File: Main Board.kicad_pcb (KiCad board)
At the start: 4 copper layers, 161 x 92 mm, 369 parts, among them J1 Motor Y, J10 CA58SUB-B, J11 PC6 EPSON MAINBOARD, J12 Y AXIS, J13 Z AXIS, J14 LED 1, J15 LED 2, J16 Power Input, J17 VS, J18 12V, J19 5V, J2 Motor Z, J20 3.3V, J21 TABLE SENSOR, J22 INPUT1, J23 INPUT2, J24 PHOTO SENSOR EMITER, J25 PHOTO SENSOR RECEIVER, J26 ANALOG, J27 INPUT3, J28 OUT1, J29 OUT2, J3 USB_B, J30 RELAY, J31 EMERGENCY, J32 EPSON POWER IN, J33 EPSON BOARD POWER, J34 Display, J35 SPI Interface, J36 I2C Interface, J37 LED4, J38 LED3, J39 Key 3, J4 SWD, J40 Key 4, J41 Key 1, J42 Key 2, J5 DEBUG, J6 LIMIT Y BACK, J7 LIMIT Y FRONT, J8 LIMIT Z UP, J9 LIMIT Z DOWN, K1 S13-24V-2C, Q1 2N7002K, Q10 2N7002K, Q11 BC817, Q12 BC817, Q13 BC817, Q14 2N7002K, Q15 2N7002K, Q16 2N7002K, Q17 BC817, Q18 2N7002K, Q19 2N7002K, Q2 2N7002K, Q20 2N7002K, Q21 2N7002K, Q3 2N7002K, Q4 2N7002K, Q5 2N7002K, Q6 2N7002K, Q7 2N7002K, Q8 YJS9435A, Q9 2N7002K, U1 TMC2209-LA, U10 74HC2G32, U11 74HC245, U12 SHTC3, U2 TMC2209-LA, U3 STM32F401VETx, U4 USBUF02W6, U5 74HC245, U6 MCP16301, U7 A4403, U8 MCP16301, U9 MCP6002-xSN, Y1 8MHz

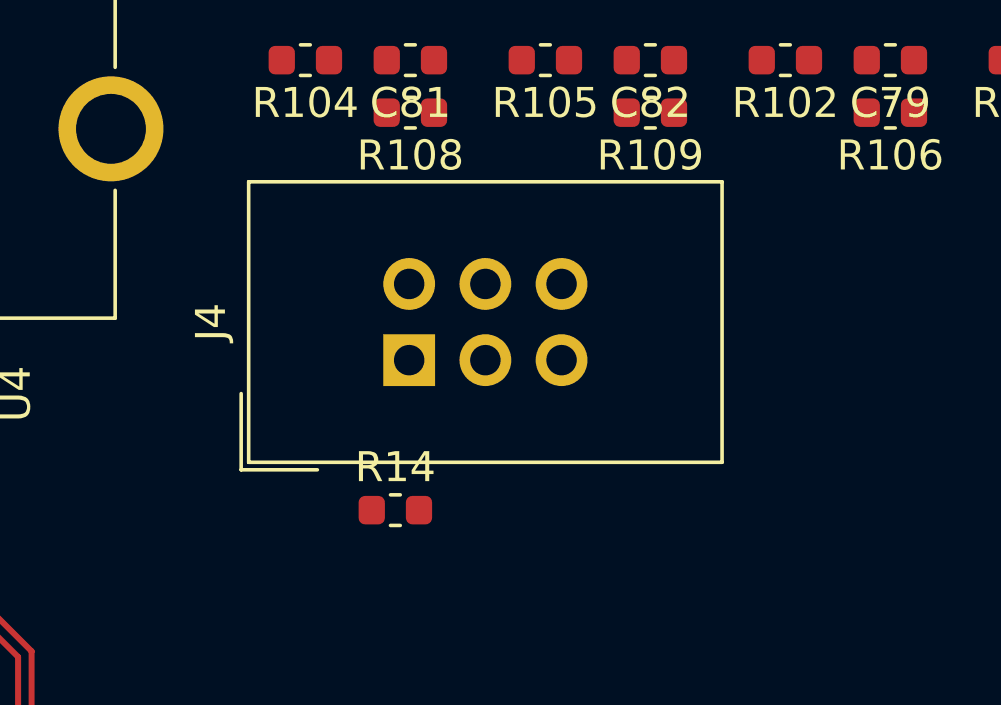
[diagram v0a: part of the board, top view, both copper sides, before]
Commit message: Change SWD IDC connector to TC2030
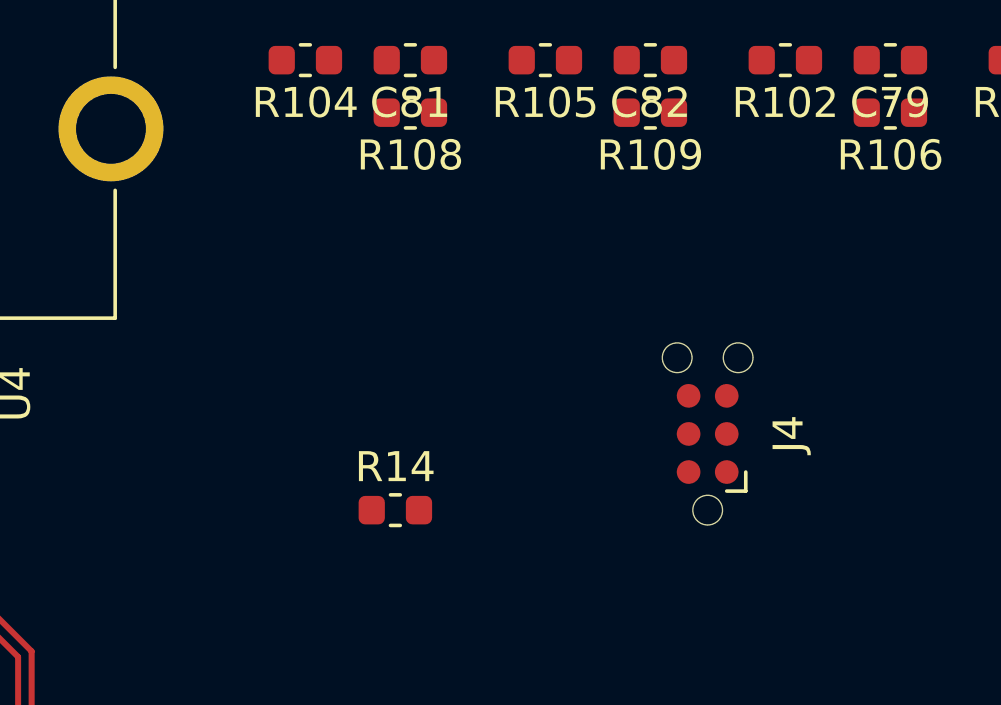
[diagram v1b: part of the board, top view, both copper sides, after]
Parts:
- J4: footprint Connector_IDC:IDC-Header_2x03_P2.54mm_Vertical -> Connector:Tag-Connect_TC2030-IDC-NL_2x03_P1.27mm_Vertical
- moved J4 10.2 mm to (156.2, 45.5)
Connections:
- J4 pad 2: NRST -> SWDIO
- J4 pad 3: SWO -> NRST
- J4 pad 4: SWDIO -> SWCLK
- J4 pad 6: SWCLK -> SWO
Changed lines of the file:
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@@
     )
   )
-  (module Connector_IDC:IDC-Header_2x03_P2.54mm_Vertical (layer F.Cu)
-    (at 146.21 43 90)
-    (descr "Through hole straight IDC box header, 2x03, 2.54mm pitch, double rows")
-    (tags "Through hole IDC box header THT 2x03 2.54mm double row")
-    (fp_text reference J4 (at 1.27 -6.604 90) (layer F.SilkS)
-      (effects (font (size 1 1) (thickness 0.15)))
-    )
-    (fp_text value SWD (at 1.27 11.684 90) (layer F.Fab)
-      (effects (font (size 1 1) (thickness 0.15)))
-    )
-    (fp_text user %R (at 1.27 2.54 90) (layer F.Fab)
-      (effects (font (size 1 1) (thickness 0.15)))
-    )
-    (fp_line (start 5.695 -5.1) (end 5.695 10.18) (layer F.Fab) (width 0.1))
-    (fp_line (start 5.145 -4.56) (end 5.145 9.62) (layer F.Fab) (width 0.1))
-    (fp_line (start -3.155 -5.1) (end -3.155 10.18) (layer F.Fab) (width 0.1))
-    (fp_line (start -2.605 -4.56) (end -2.605 0.29) (layer F.Fab) (width 0.1))
-    (fp_line (start -2.605 4.79) (end -2.605 9.62) (layer F.Fab) (width 0.1))
-    (fp_line (start -2.605 0.29) (end -3.155 0.29) (layer F.Fab) (width 0.1))
-    (fp_line (start -2.605 4.79) (end -3.155 4.79) (layer F.Fab) (width 0.1))
-    (fp_line (start 5.695 -5.1) (end -3.155 -5.1) (layer F.Fab) (width 0.1))
-    (fp_line (start 5.145 -4.56) (end -2.605 -4.56) (layer F.Fab) (width 0.1))
-    (fp_line (start 5.695 10.18) (end -3.155 10.18) (layer F.Fab) (width 0.1))
-    (fp_line (start 5.145 9.62) (end -2.605 9.62) (layer F.Fab) (width 0.1))
-    (fp_line (start 5.695 -5.1) (end 5.145 -4.56) (layer F.Fab) (width 0.1))
-    (fp_line (start 5.695 10.18) (end 5.145 9.62) (layer F.Fab) (width 0.1))
-    (fp_line (start -3.155 -5.1) (end -2.605 -4.56) (layer F.Fab) (width 0.1))
-    (fp_line (start -3.155 10.18) (end -2.605 9.62) (layer F.Fab) (width 0.1))
-    (fp_line (start 5.95 -5.35) (end 5.95 10.43) (layer F.CrtYd) (width 0.05))
-    (fp_line (start 5.95 10.43) (end -3.41 10.43) (layer F.CrtYd) (width 0.05))
-    (fp_line (start -3.41 10.43) (end -3.41 -5.35) (layer F.CrtYd) (width 0.05))
-    (fp_line (start -3.41 -5.35) (end 5.95 -5.35) (layer F.CrtYd) (width 0.05))
-    (fp_line (start 5.945 -5.35) (end 5.945 10.43) (layer F.SilkS) (width 0.12))
-    (fp_line (start 5.945 10.43) (end -3.405 10.43) (layer F.SilkS) (width 0.12))
-    (fp_line (start -3.405 10.43) (end -3.405 -5.35) (layer F.SilkS) (width 0.12))
-    (fp_line (start -3.405 -5.35) (end 5.945 -5.35) (layer F.SilkS) (width 0.12))
-    (fp_line (start -3.655 -5.6) (end -3.655 -3.06) (layer F.SilkS) (width 0.12))
-    (fp_line (start -3.655 -5.6) (end -1.115 -5.6) (layer F.SilkS) (width 0.12))
-    (pad 1 thru_hole rect (at 0 0 90) (size 1.7272 1.7272) (drill 1.016) (layers *.Cu *.Mask)
-      (net 66 "Net-(J4-Pad1)"))
-    (pad 2 thru_hole oval (at 2.54 0 90) (size 1.7272 1.7272) (drill 1.016) (layers *.Cu *.Mask)
-      (net 67 NRST))
-    (pad 3 thru_hole oval (at 0 2.54 90) (size 1.7272 1.7272) (drill 1.016) (layers *.Cu *.Mask)
-      (net 68 SWO))
-    (pad 4 thru_hole oval (at 2.54 2.54 90) (size 1.7272 1.7272) (drill 1.016) (layers *.Cu *.Mask)
-      (net 69 SWDIO))
-    (pad 5 thru_hole oval (at 0 5.08 90) (size 1.7272 1.7272) (drill 1.016) (layers *.Cu *.Mask)
-      (net 2 GND))
-    (pad 6 thru_hole oval (at 2.54 5.08 90) (size 1.7272 1.7272) (drill 1.016) (layers *.Cu *.Mask)
-      (net 70 SWCLK))
-    (model ${KISYS3DMOD}/Connector_IDC.3dshapes/IDC-Header_2x03_P2.54mm_Vertical.wrl
-      (at (xyz 0 0 0))
-      (scale (xyz 1 1 1))
-      (rotate (xyz 0 0 0))
-    )
-  )
   (module Connector_JST:JST_PH_B3B-PH-K_1x03_P2.00mm_Vertical (layer F.Cu)
     (at 89 28)
@@
     )
   )
+  (module Connector:Tag-Connect_TC2030-IDC-NL_2x03_P1.27mm_Vertical (layer F.Cu)
+    (at 156.16 45.46 90)
+    (descr "Tag-Connect programming header; http://www.tag-connect.com/Materials/TC2030-IDC-NL.pdf")
+    (tags "tag connect programming header pogo pins")
+    (attr virtual)
+    (fp_text reference J4 (at 0 2.7 90) (layer F.SilkS)
+      (effects (font (size 1 1) (thickness 0.15)))
+    )
+    (fp_text value SWD (at 0 -2.3 90) (layer F.Fab)
+      (effects (font (size 1 1) (thickness 0.15)))
+    )
+    (fp_line (start -1.905 1.27) (end -1.905 0.635) (layer F.SilkS) (width 0.12))
+    (fp_line (start -1.27 1.27) (end -1.905 1.27) (layer F.SilkS) (width 0.12))
+    (fp_line (start -3.5 2) (end -3.5 -2) (layer F.CrtYd) (width 0.05))
+    (fp_line (start 3.5 2) (end -3.5 2) (layer F.CrtYd) (width 0.05))
+    (fp_line (start 3.5 -2) (end 3.5 2) (layer F.CrtYd) (width 0.05))
+    (fp_line (start -3.5 -2) (end 3.5 -2) (layer F.CrtYd) (width 0.05))
+    (fp_text user %R (at 0 0 90) (layer F.Fab)
+      (effects (font (size 1 1) (thickness 0.15)))
+    )
+    (fp_line (start -1.27 0.635) (end -1.27 -0.635) (layer Dwgs.User) (width 0.1))
+    (fp_line (start 1.27 0.635) (end -1.27 0.635) (layer Dwgs.User) (width 0.1))
+    (fp_line (start 1.27 -0.635) (end 1.27 0.635) (layer Dwgs.User) (width 0.1))
+    (fp_line (start -1.27 -0.635) (end 1.27 -0.635) (layer Dwgs.User) (width 0.1))
+    (fp_line (start -1.27 0.635) (end 0 -0.635) (layer Dwgs.User) (width 0.1))
+    (fp_line (start -1.27 0) (end -0.635 -0.635) (layer Dwgs.User) (width 0.1))
+    (fp_line (start -0.635 0.635) (end 0.635 -0.635) (layer Dwgs.User) (width 0.1))
+    (fp_line (start 0 0.635) (end 1.27 -0.635) (layer Dwgs.User) (width 0.1))
+    (fp_line (start 0.635 0.635) (end 1.27 0) (layer Dwgs.User) (width 0.1))
+    (fp_text user KEEPOUT (at 0 0 90) (layer Cmts.User)
+      (effects (font (size 0.4 0.4) (thickness 0.07)))
+    )
+    (pad "" np_thru_hole circle (at 2.54 -1.016 90) (size 0.9906 0.9906) (drill 0.9906) (layers *.Cu *.Mask))
+    (pad "" np_thru_hole circle (at 2.54 1.016 90) (size 0.9906 0.9906) (drill 0.9906) (layers *.Cu *.Mask))
+    (pad "" np_thru_hole circle (at -2.54 0 90) (size 0.9906 0.9906) (drill 0.9906) (layers *.Cu *.Mask))
+    (pad 1 connect circle (at -1.27 0.635 90) (size 0.7874 0.7874) (layers F.Cu F.Mask)
+      (net 66 "Net-(J4-Pad1)"))
+    (pad 2 connect circle (at -1.27 -0.635 90) (size 0.7874 0.7874) (layers F.Cu F.Mask)
+      (net 69 SWDIO))
+    (pad 3 connect circle (at 0 0.635 90) (size 0.7874 0.7874) (layers F.Cu F.Mask)
+      (net 67 NRST))
+    (pad 4 connect circle (at 0 -0.635 90) (size 0.7874 0.7874) (layers F.Cu F.Mask)
+      (net 70 SWCLK))
+    (pad 5 connect circle (at 1.27 0.635 90) (size 0.7874 0.7874) (layers F.Cu F.Mask)
+      (net 2 GND))
+    (pad 6 connect circle (at 1.27 -0.635 90) (size 0.7874 0.7874) (layers F.Cu F.Mask)
+      (net 68 SWO))
+  )
   (gr_line (start 204 116) (end 204 24) (layer Edge.Cuts) (width 0.05))

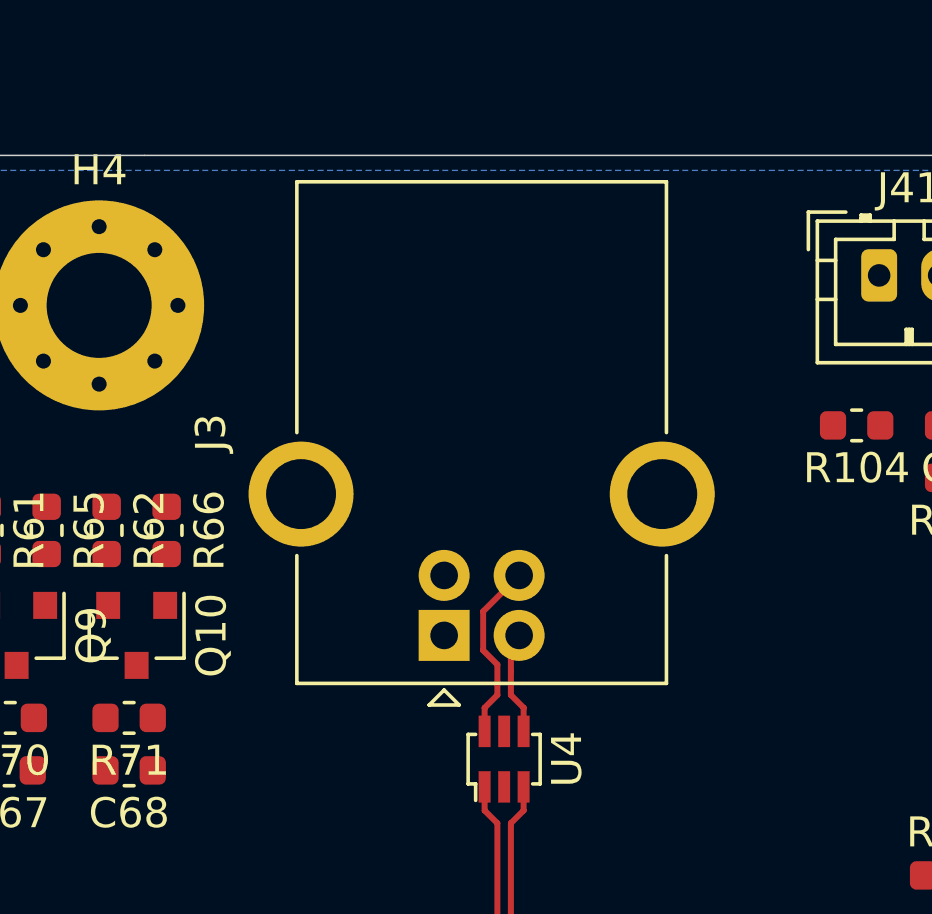
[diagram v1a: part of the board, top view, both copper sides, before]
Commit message: Change USB Horizontal to Vertical
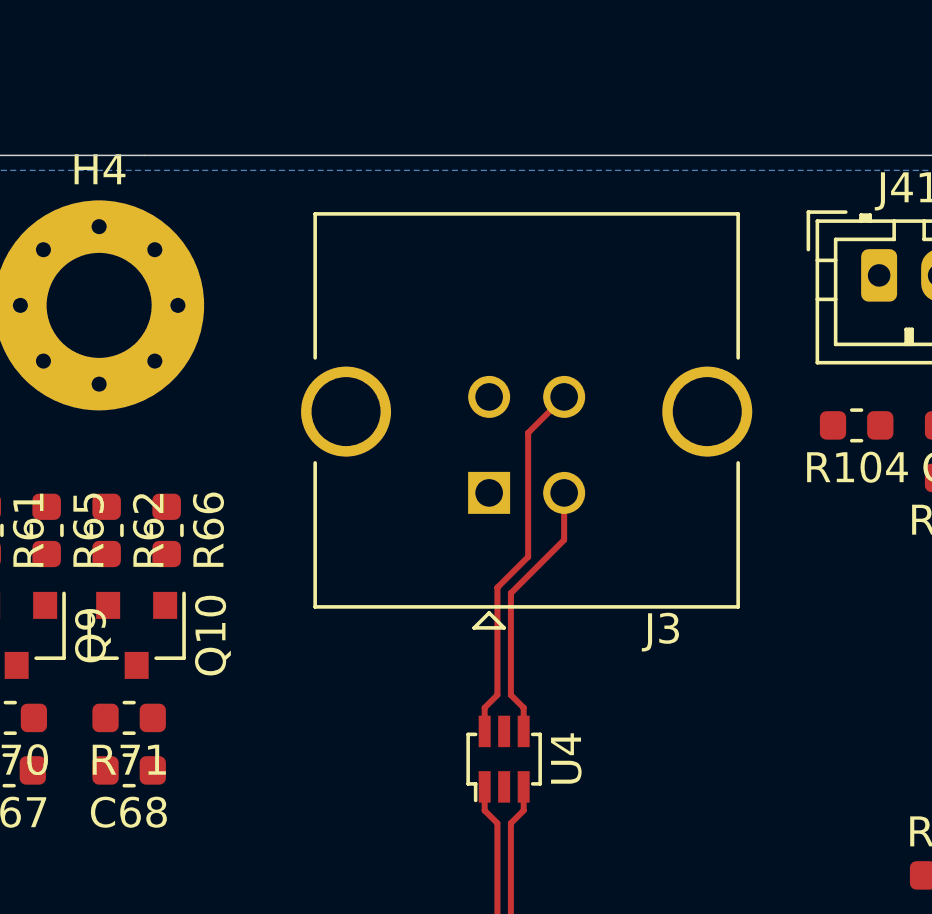
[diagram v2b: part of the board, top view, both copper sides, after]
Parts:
- J3: footprint Connector_USB:USB_B_OST_USB-B1HSxx_Horizontal -> Connector_USB:USB_B_TE_5787834_Vertical
- moved J3 4.98 mm to (130.5, 35.2), turned to 180 degrees
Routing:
- net /Microcontroller/D+: track 6.07 -> 12.2 mm
- net /Microcontroller/D-: track 3.49 -> 8.86 mm
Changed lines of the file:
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@@
   )
   (setup
-    (last_trace_width 0.25)
+    (last_trace_width 0.2)
     (user_trace_width 0.2)
     (user_trace_width 0.254)
@@
     (add_net Z_STEP)
   )
+  (module Connector_USB:USB_B_TE_5787834_Vertical (layer F.Cu)
+    (at 130.5 35.25 180)
+    (descr http://www.mouser.com/ds/2/418/NG_CD_5787834_A4-669110.pdf)
+    (tags "USB_B USB B vertical female connector")
+    (fp_text reference J3 (at -5.8 -4.55) (layer F.SilkS)
+      (effects (font (size 1 1) (thickness 0.15)))
+    )
+    (fp_text value USB_B (at -1.25 10.25) (layer F.Fab)
+      (effects (font (size 1 1) (thickness 0.15)))
+    )
+    (fp_text user %R (at -1.2 6.4) (layer F.Fab)
+      (effects (font (size 1 1) (thickness 0.15)))
+    )
+    (fp_line (start -8.3 1) (end -8.3 -3.8) (layer F.SilkS) (width 0.12))
+    (fp_line (start -8.3 9.3) (end -8.3 4.5) (layer F.SilkS) (width 0.12))
+    (fp_line (start 5.8 9.3) (end -8.3 9.3) (layer F.SilkS) (width 0.12))
+    (fp_line (start 5.8 4.5) (end 5.8 9.3) (layer F.SilkS) (width 0.12))
+    (fp_line (start 5.8 -3.8) (end 5.8 1) (layer F.SilkS) (width 0.12))
+    (fp_line (start -8.3 -3.8) (end 5.8 -3.8) (layer F.SilkS) (width 0.12))
+    (fp_line (start -0.5 -4.5) (end 0 -4) (layer F.SilkS) (width 0.12))
+    (fp_line (start 0.5 -4.5) (end -0.5 -4.5) (layer F.SilkS) (width 0.12))
+    (fp_line (start 0 -4) (end 0.5 -4.5) (layer F.SilkS) (width 0.12))
+    (fp_line (start 5 -3.75) (end 5.75 -3) (layer F.Fab) (width 0.1))
+    (fp_line (start -8.25 -3.75) (end 5 -3.75) (layer F.Fab) (width 0.1))
+    (fp_line (start 5.75 -3) (end 5.75 9.25) (layer F.Fab) (width 0.1))
+    (fp_line (start 5.75 9.25) (end -8.25 9.25) (layer F.Fab) (width 0.1))
+    (fp_line (start -8.25 9.25) (end -8.25 -3.75) (layer F.Fab) (width 0.1))
+    (fp_line (start -9 -4) (end 6.5 -4) (layer F.CrtYd) (width 0.05))
+    (fp_line (start -9 -4) (end -9 9.5) (layer F.CrtYd) (width 0.05))
+    (fp_line (start 6.5 9.5) (end 6.5 -4) (layer F.CrtYd) (width 0.05))
+    (fp_line (start 6.5 9.5) (end -9 9.5) (layer F.CrtYd) (width 0.05))
+    (pad 5 thru_hole circle (at 4.77 2.71 180) (size 3 3) (drill 2.3) (layers *.Cu *.Mask)
+      (net 65 "Net-(J3-Pad5)"))
+    (pad 4 thru_hole circle (at 0 3.2 180) (size 1.4 1.4) (drill 0.92) (layers *.Cu *.Mask)
+      (net 2 GND))
+    (pad 3 thru_hole circle (at -2.5 3.2 180) (size 1.4 1.4) (drill 0.92) (layers *.Cu *.Mask)
+      (net 199 /Microcontroller/D+))
+    (pad 1 thru_hole rect (at 0 0 180) (size 1.4 1.4) (drill 0.92) (layers *.Cu *.Mask)
+      (net 64 "Net-(J3-Pad1)"))
+    (pad 5 thru_hole circle (at -7.27 2.71 180) (size 3 3) (drill 2.3) (layers *.Cu *.Mask)
+      (net 65 "Net-(J3-Pad5)"))
+    (pad 2 thru_hole circle (at -2.5 0 180) (size 1.4 1.4) (drill 0.92) (layers *.Cu *.Mask)
+      (net 198 /Microcontroller/D-))
+    (model "${KIPRJMOD}/Parts Library/packages3d/USB_THT/USB_Type_B_Vertical_c-5787834-1-c-3d.stp"
+      (offset (xyz -1.25 -1.6 15.3))
+      (scale (xyz 1 1 1))
+      (rotate (xyz 0 0 0))
+    )
+  )
   (module footprints:THT_FPC_r1.0mm_11pin_vertical (layer F.Cu)
     (at 46 91 270)
@@
     )
   )
-  (module Connector_USB:USB_B_OST_USB-B1HSxx_Horizontal (layer F.Cu)
-    (at 129 40 90)
-    (descr "USB B receptacle, Horizontal, through-hole, http://www.on-shore.com/wp-content/uploads/2015/09/usb-b1hsxx.pdf")
-    (tags "USB-B receptacle horizontal through-hole")
-    (fp_text reference J3 (at 6.76 -7.77 90) (layer F.SilkS)
-      (effects (font (size 1 1) (thickness 0.15)))
-    )
-    (fp_text value USB_B (at 6.76 10.27 90) (layer F.Fab)
-      (effects (font (size 1 1) (thickness 0.15)))
-    )
-    (fp_line (start -0.49 -4.8) (end 15.01 -4.8) (layer F.Fab) (width 0.1))
-    (fp_line (start 15.01 -4.8) (end 15.01 7.3) (layer F.Fab) (width 0.1))
-    (fp_line (start 15.01 7.3) (end -1.49 7.3) (layer F.Fab) (width 0.1))
-    (fp_line (start -1.49 7.3) (end -1.49 -3.8) (layer F.Fab) (width 0.1))
-    (fp_line (start -1.49 -3.8) (end -0.49 -4.8) (layer F.Fab) (width 0.1))
-    (fp_line (start 2.66 -4.91) (end -1.6 -4.91) (layer F.SilkS) (width 0.12))
-    (fp_line (start -1.6 -4.91) (end -1.6 7.41) (layer F.SilkS) (width 0.12))
-    (fp_line (start -1.6 7.41) (end 2.66 7.41) (layer F.SilkS) (width 0.12))
-    (fp_line (start 6.76 -4.91) (end 15.12 -4.91) (layer F.SilkS) (width 0.12))
-    (fp_line (start 15.12 -4.91) (end 15.12 7.41) (layer F.SilkS) (width 0.12))
-    (fp_line (start 15.12 7.41) (end 6.76 7.41) (layer F.SilkS) (width 0.12))
-    (fp_line (start -1.82 0) (end -2.32 -0.5) (layer F.SilkS) (width 0.12))
-    (fp_line (start -2.32 -0.5) (end -2.32 0.5) (layer F.SilkS) (width 0.12))
-    (fp_line (start -2.32 0.5) (end -1.82 0) (layer F.SilkS) (width 0.12))
-    (fp_line (start -1.99 -7.02) (end -1.99 9.52) (layer F.CrtYd) (width 0.05))
-    (fp_line (start -1.99 9.52) (end 15.51 9.52) (layer F.CrtYd) (width 0.05))
-    (fp_line (start 15.51 9.52) (end 15.51 -7.02) (layer F.CrtYd) (width 0.05))
-    (fp_line (start 15.51 -7.02) (end -1.99 -7.02) (layer F.CrtYd) (width 0.05))
-    (fp_text user %R (at 6.76 1.25 90) (layer F.Fab)
-      (effects (font (size 1 1) (thickness 0.15)))
-    )
-    (pad 1 thru_hole rect (at 0 0 90) (size 1.7 1.7) (drill 0.92) (layers *.Cu *.Mask)
-      (net 64 "Net-(J3-Pad1)"))
-    (pad 2 thru_hole circle (at 0 2.5 90) (size 1.7 1.7) (drill 0.92) (layers *.Cu *.Mask)
-      (net 198 /Microcontroller/D-))
-    (pad 3 thru_hole circle (at 2 2.5 90) (size 1.7 1.7) (drill 0.92) (layers *.Cu *.Mask)
-      (net 199 /Microcontroller/D+))
-    (pad 4 thru_hole circle (at 2 0 90) (size 1.7 1.7) (drill 0.92) (layers *.Cu *.Mask)
-      (net 2 GND))
-    (pad 5 thru_hole circle (at 4.71 -4.77 90) (size 3.5 3.5) (drill 2.33) (layers *.Cu *.Mask)
-      (net 65 "Net-(J3-Pad5)"))
-    (pad 5 thru_hole circle (at 4.71 7.27 90) (size 3.5 3.5) (drill 2.33) (layers *.Cu *.Mask)
-      (net 65 "Net-(J3-Pad5)"))
-    (model "${KIPRJMOD}/Parts Library/packages3d/USB_THT/USB_Type_B_Horizontal.stp"
-      (at (xyz 0 0 0))
-      (scale (xyz 1 1 1))
-      (rotate (xyz 0 0 -90))
-    )
-  )
   (module Connector_JST:JST_PH_B3B-PH-K_1x03_P2.00mm_Vertical (layer F.Cu)
     (at 89 28)
@@
   (segment (start 60.7875 46.5) (end 61.75 46.5) (width 0.3048) (layer F.Cu) (net 193))
   (segment (start 63 43.3) (end 65.4 43.3) (width 0.3048) (layer F.Cu) (net 193))
-  (segment (start 131.225 40.275) (end 131.5 40) (width 0.25) (layer F.Cu) (net 198))
-  (segment (start 131.65 42.412499) (end 131.225 41.987499) (width 0.2) (layer F.Cu) (net 198))
-  (segment (start 131.65 43.2) (end 131.65 42.412499) (width 0.2) (layer F.Cu) (net 198))
-  (segment (start 131.225 41.987499) (end 131.225 41.2) (width 0.2) (layer F.Cu) (net 198))
-  (segment (start 131.225 41.2) (end 131.225 40.275) (width 0.2) (layer F.Cu) (net 198))
-  (segment (start 130.3 39.2) (end 131.5 38) (width 0.2) (layer F.Cu) (net 199))
-  (segment (start 130.35 42.412499) (end 130.775 41.987499) (width 0.2) (layer F.Cu) (net 199))
-  (segment (start 130.775 41.987499) (end 130.775 40.975) (width 0.2) (layer F.Cu) (net 199))
-  (segment (start 130.35 43.2) (end 130.35 42.412499) (width 0.2) (layer F.Cu) (net 199))
-  (segment (start 130.3 40.5) (end 130.3 39.2) (width 0.2) (layer F.Cu) (net 199))
-  (segment (start 130.775 40.975) (end 130.3 40.5) (width 0.2) (layer F.Cu) (net 199))
+  (segment (start 133 36.8182) (end 131.225 38.5932) (width 0.2) (layer F.Cu) (net 198))
+  (segment (start 133 35.25) (end 133 36.8182) (width 0.2) (layer F.Cu) (net 198))
+  (segment (start 131.65 42.412499) (end 131.65 43.2) (width 0.2) (layer F.Cu) (net 198))
+  (segment (start 131.225 38.5932) (end 131.225 41.987499) (width 0.2) (layer F.Cu) (net 198))
+  (segment (start 131.225 41.987499) (end 131.65 42.412499) (width 0.2) (layer F.Cu) (net 198))
+  (segment (start 130.35 42.412499) (end 130.35 43.2) (width 0.2) (layer F.Cu) (net 199))
+  (segment (start 131.8 33.25) (end 131.8 37.3818) (width 0.2) (layer F.Cu) (net 199))
+  (segment (start 133 32.05) (end 131.8 33.25) (width 0.2) (layer F.Cu) (net 199))
+  (segment (start 131.8 37.3818) (end 130.775 38.4068) (width 0.2) (layer F.Cu) (net 199))
+  (segment (start 130.775 38.4068) (end 130.775 41.987499) (width 0.2) (layer F.Cu) (net 199))
+  (segment (start 130.775 41.987499) (end 130.35 42.412499) (width 0.2) (layer F.Cu) (net 199))
   (segment (start 131.65 45.837501) (end 131.65 45.05) (width 0.2) (layer F.Cu) (net 223))
   (segment (start 131.225 46.262501) (end 131.65 45.837501) (width 0.2) (layer F.Cu) (net 223))
